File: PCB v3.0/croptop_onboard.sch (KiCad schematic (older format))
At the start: 100 parts, among them J15 TSM-112-01-L-DV, J16 DM3D-SF, Q4 BSS138, Q5 BSS138, Q6 BSS138, SW2 SW_Push, SW3 SW_Push, SW4 SW_Push, U30 TPD4E1U06DBV, U31 TPD4E1U06DBV, U32 AP22802AW5, U33 AP22802AW5, U34 TPD4E1U06DBV, U35 TPD4E1U06DBV, U36 AP22802AW5, U37 TPD4E1U06DBV, U38 TPD4E1U06DBV, U39 LIS3DSHTR, U40 CAM-M8C-0, U41 Si7006-A20

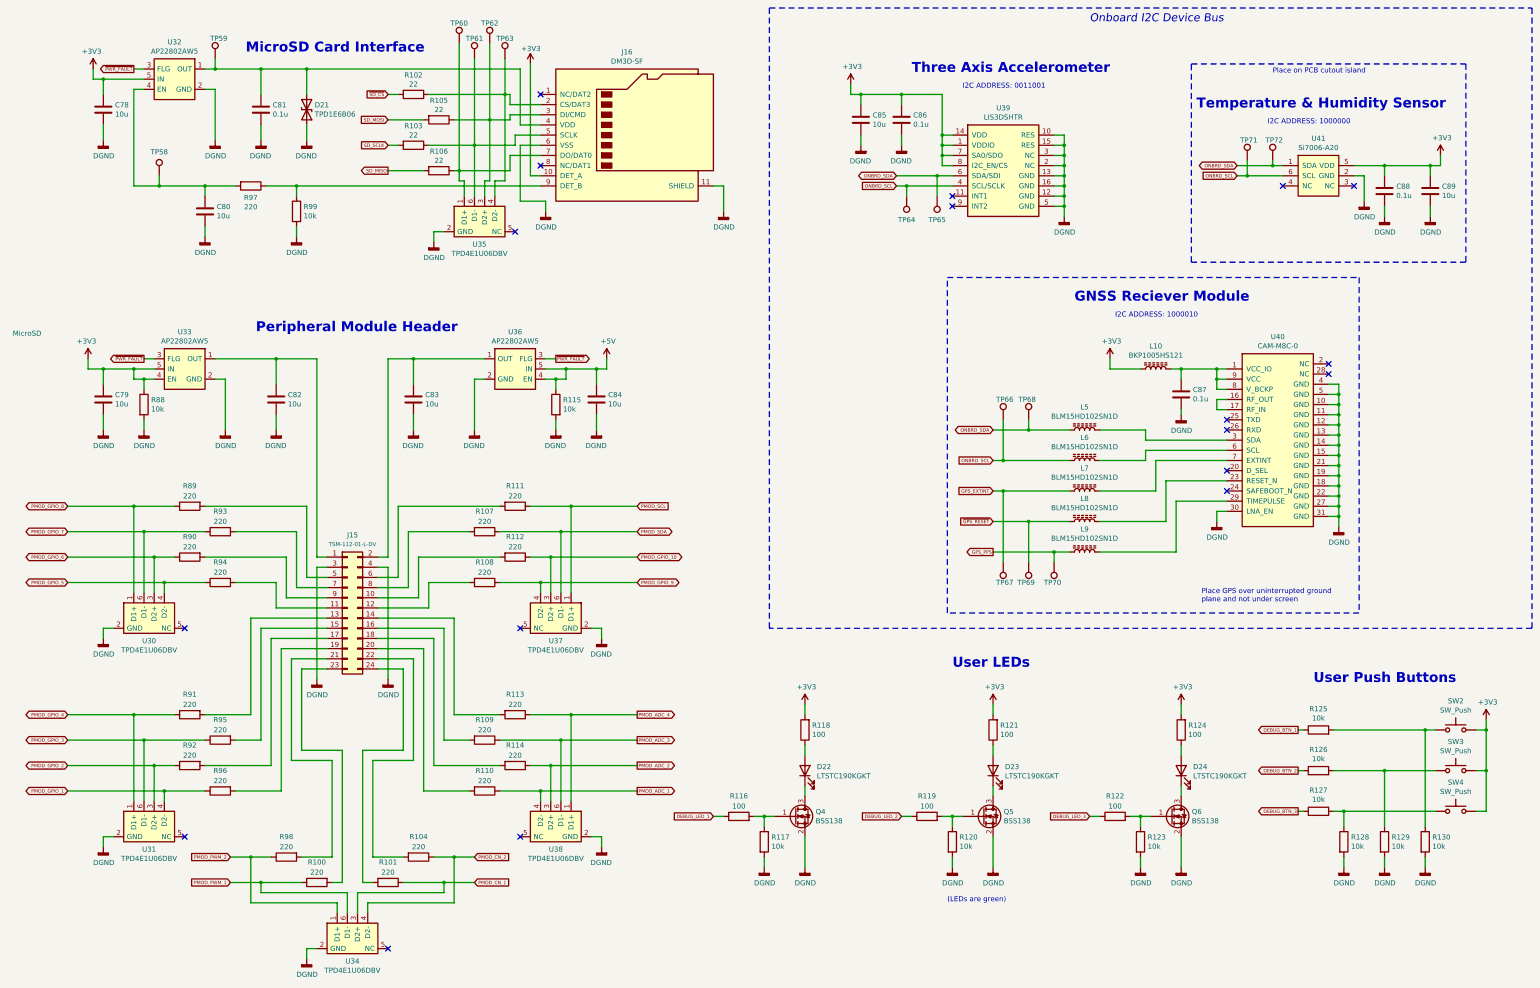
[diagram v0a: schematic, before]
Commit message: Updated PCB dimensions for Nextion screen, deleted old files
- Updated PCB v3.0 to use the Nextion screen mounting and connectors
- Deleted old I2CDriver files from /Software/
- Deleted unused /Software/Readme
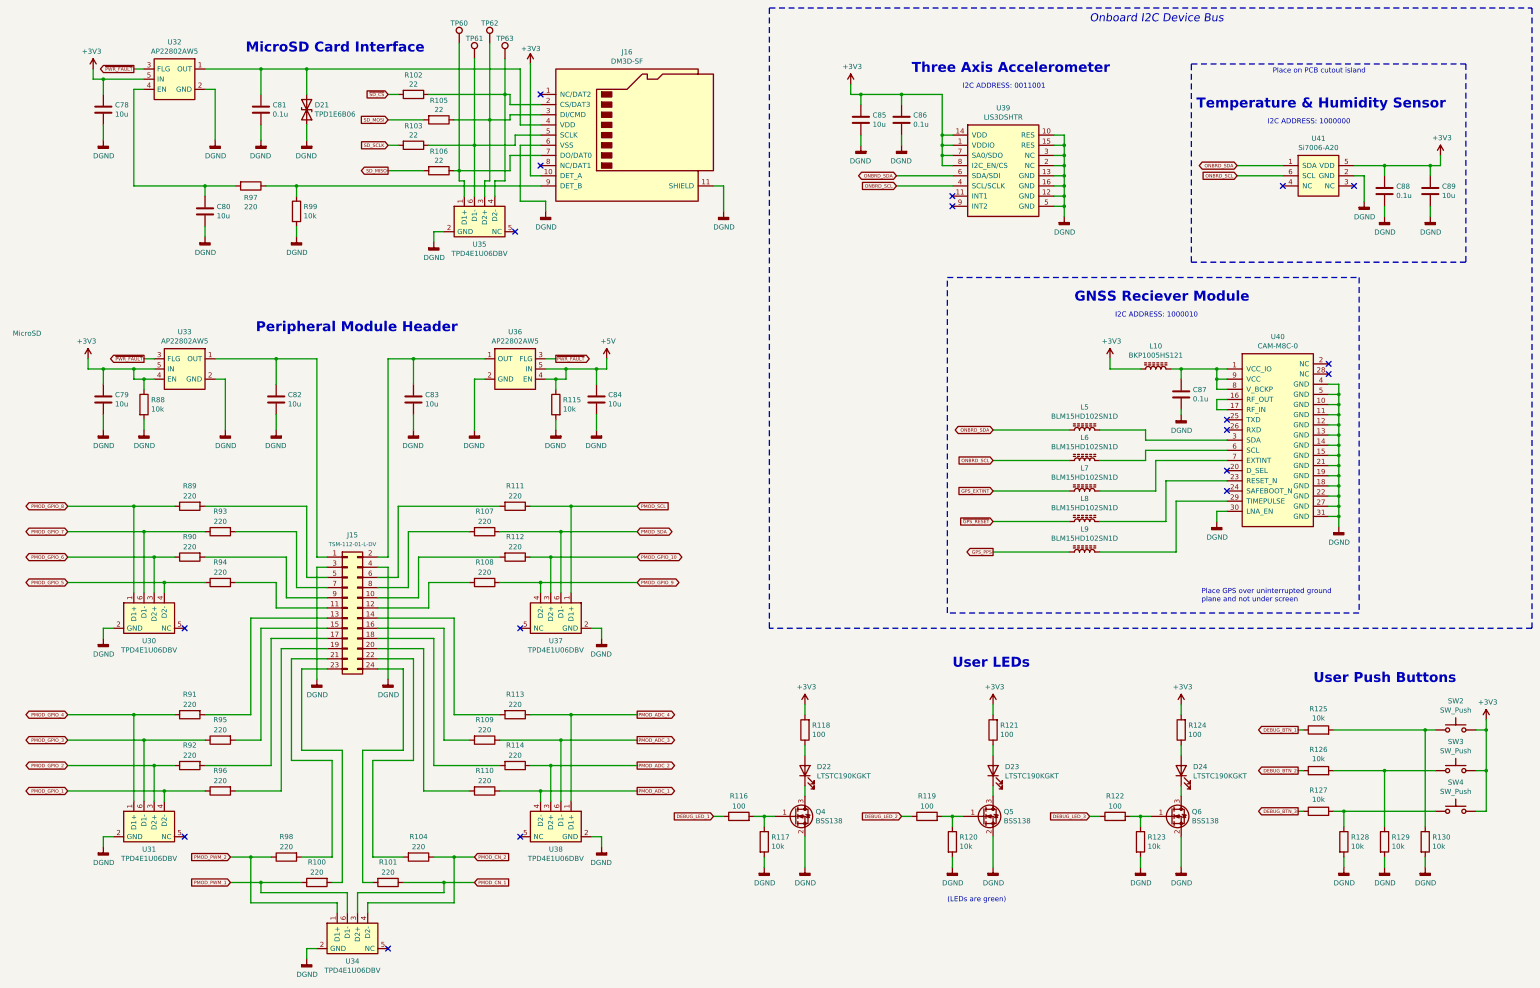
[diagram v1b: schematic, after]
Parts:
- removed TP58, TP59, TP64, TP65, TP66, TP67, TP68, TP69, TP70, TP71, TP72: TestPoint, TestPoint:TestPoint_Pad_D1.0mm, symbol Connector:TestPoint
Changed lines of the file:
@@
 $EndComp
 $Comp
-L CropTop:Si7006-A20 U41
-U 1 1 5CA090A6
-P 14050 2350
-F 0 "U41" H 14050 2717 50  0000 C CNN
-F 1 "Si7006-A20" H 14050 2626 50  0000 C CNN
-F 2 "croptop:SI7006" H 14050 2350 50  0001 C CNN
-F 3 "https://www.silabs.com/documents/public/data-sheets/Si7006-A20.pdf" H 14050 2350 50  0001 C CNN
-F 4 "SI7006-A20-IMR" H 14050 2350 50  0001 C CNN "MPN"
-	1    14050 2350
-	1    0    0    -1
-$EndComp
-$Comp
 L CropTop:DGND #PWR0227
 U 1 1 5CA022AE
@@
 	8100 2450 8200 2450
 $Comp
-L Connector:TestPoint TP?
-U 1 1 5CB78F40
-P 2650 2350
-AR Path="/64809F0C/5CB78F40" Ref="TP?"  Part="1"
-AR Path="/66A12230/5CB78F40" Ref="TP58"  Part="1"
-F 0 "TP58" H 2650 2584 50  0000 C CNN
-F 1 "TestPoint" H 2708 2379 50  0001 L CNN
-F 2 "TestPoint:TestPoint_Pad_D1.0mm" H 2850 2350 50  0001 C CNN
-F 3 "" H 2850 2350 50  0001 C CNN
-	1    2650 2350
-	1    0    0    -1
-$EndComp
-Wire Wire Line
-	2650 2350 2650 2450
-$Comp
 L CropTop:Micro_SD_Card_Det_0 J16
 U 1 1 5CBDF819
@@
 	2100 1850 2100 2000
 $Comp
-L Connector:TestPoint TP?
-U 1 1 5FDFF2C7
-P 3200 1200
-AR Path="/64809F0C/5FDFF2C7" Ref="TP?"  Part="1"
-AR Path="/66A12230/5FDFF2C7" Ref="TP59"  Part="1"
-AR Path="/64807BBC/5FDFF2C7" Ref="TP?"  Part="1"
-F 0 "TP59" H 3150 1400 50  0000 L CNN
-F 1 "TestPoint" H 3258 1229 50  0001 L CNN
-F 2 "TestPoint:TestPoint_Pad_D1.0mm" H 3400 1200 50  0001 C CNN
-F 3 "" H 3400 1200 50  0001 C CNN
-	1    3200 1200
-	1    0    0    -1
-$EndComp
-Wire Wire Line
-	3200 1200 3200 1300
-$Comp
 L CropTop:AP22802AW5 U?
 U 1 1 5FDFF2D1
@@
 Text GLabel 13250 2350 0    33   Input ~ 0
 ONBRD_SCL
-Wire Wire Line
-	13250 2250 13600 2250
-Wire Wire Line
-	13250 2350 13350 2350
 $Comp
 L CropTop:DGND #PWR?
@@
 Wire Wire Line
 	13050 5650 13050 5750
-Wire Wire Line
-	9900 2450 10000 2450
 $Comp
 L Device:L_Core_Ferrite L8
@@
 Wire Wire Line
 	12650 6050 11900 6050
-$Comp
-L Connector:TestPoint TP?
-U 1 1 5F92792B
-P 10950 6150
-AR Path="/64809F0C/5F92792B" Ref="TP?"  Part="1"
-AR Path="/66A12230/5F92792B" Ref="TP67"  Part="1"
-AR Path="/64807BBC/5F92792B" Ref="TP?"  Part="1"
-F 0 "TP67" H 10850 6350 50  0000 L CNN
-F 1 "TestPoint" H 11008 6179 50  0001 L CNN
-F 2 "TestPoint:TestPoint_Pad_D1.0mm" H 11150 6150 50  0001 C CNN
-F 3 "" H 11150 6150 50  0001 C CNN
-	1    10950 6150
-	-1   0    0    1
-$EndComp
-$Comp
-L Connector:TestPoint TP?
-U 1 1 5F927A3B
-P 10950 4750
-AR Path="/64809F0C/5F927A3B" Ref="TP?"  Part="1"
-AR Path="/66A12230/5F927A3B" Ref="TP66"  Part="1"
-AR Path="/64807BBC/5F927A3B" Ref="TP?"  Part="1"
-F 0 "TP66" H 10850 4950 50  0000 L CNN
-F 1 "TestPoint" H 11008 4779 50  0001 L CNN
-F 2 "TestPoint:TestPoint_Pad_D1.0mm" H 11150 4750 50  0001 C CNN
-F 3 "" H 11150 4750 50  0001 C CNN
-	1    10950 4750
-	-1   0    0    -1
-$EndComp
-$Comp
-L Connector:TestPoint TP?
-U 1 1 5F927CC0
-P 11200 6150
-AR Path="/64809F0C/5F927CC0" Ref="TP?"  Part="1"
-AR Path="/66A12230/5F927CC0" Ref="TP69"  Part="1"
-AR Path="/64807BBC/5F927CC0" Ref="TP?"  Part="1"
-F 0 "TP69" H 11310 6350 50  0000 R CNN
-F 1 "TestPoint" H 11258 6179 50  0001 L CNN
-F 2 "TestPoint:TestPoint_Pad_D1.0mm" H 11400 6150 50  0001 C CNN
-F 3 "" H 11400 6150 50  0001 C CNN
-	1    11200 6150
-	-1   0    0    1
-$EndComp
 Wire Wire Line
 	12450 5150 12450 5450
@@
 ~GPS_RESET
 $Comp
-L Connector:TestPoint TP?
-U 1 1 60F3FF7D
-P 10000 2550
-AR Path="/64809F0C/60F3FF7D" Ref="TP?"  Part="1"
-AR Path="/66A12230/60F3FF7D" Ref="TP64"  Part="1"
-AR Path="/64807BBC/60F3FF7D" Ref="TP?"  Part="1"
-F 0 "TP64" H 10000 2783 50  0000 C CNN
-F 1 "TestPoint" H 10058 2579 50  0001 L CNN
-F 2 "TestPoint:TestPoint_Pad_D1.0mm" H 10200 2550 50  0001 C CNN
-F 3 "" H 10200 2550 50  0001 C CNN
-	1    10000 2550
-	-1   0    0    1
-$EndComp
-Wire Wire Line
-	10000 2550 10000 2450
-Wire Wire Line
-	10300 2550 10300 2350
-$Comp
 L Device:Q_NMOS_GSD Q5
 U 1 1 6149971C
@@
 	2500 1500 2400 1500
 Wire Wire Line
-	2400 2450 2650 2450
-Wire Wire Line
 	2400 1500 2400 2450
 Wire Wire Line
@@
 	11550 2050 11550 2150
 Wire Wire Line
-	3200 1300 3650 1300
-Wire Wire Line
 	6300 2350 6400 2350
 Connection ~ 3650 1300
@@
 	4100 1550 4100 1300
 Connection ~ 4100 1300
-$Comp
-L Connector:TestPoint TP?
-U 1 1 5D227D71
-P 10300 2550
-AR Path="/64809F0C/5D227D71" Ref="TP?"  Part="1"
-AR Path="/66A12230/5D227D71" Ref="TP65"  Part="1"
-AR Path="/64807BBC/5D227D71" Ref="TP?"  Part="1"
-F 0 "TP65" H 10300 2783 50  0000 C CNN
-F 1 "TestPoint" H 10358 2579 50  0001 L CNN
-F 2 "TestPoint:TestPoint_Pad_D1.0mm" H 10500 2550 50  0001 C CNN
-F 3 "" H 10500 2550 50  0001 C CNN
-	1    10300 2550
-	-1   0    0    1
-$EndComp
-$Comp
-L Connector:TestPoint TP?
-U 1 1 5E1D1600
-P 13350 2200
-AR Path="/64809F0C/5E1D1600" Ref="TP?"  Part="1"
-AR Path="/66A12230/5E1D1600" Ref="TP71"  Part="1"
-AR Path="/64807BBC/5E1D1600" Ref="TP?"  Part="1"
-F 0 "TP71" H 13250 2400 50  0000 L CNN
-F 1 "TestPoint" H 13408 2229 50  0001 L CNN
-F 2 "TestPoint:TestPoint_Pad_D1.0mm" H 13550 2200 50  0001 C CNN
-F 3 "" H 13550 2200 50  0001 C CNN
-	1    13350 2200
-	-1   0    0    -1
-$EndComp
-$Comp
-L Connector:TestPoint TP?
-U 1 1 5E1D1607
-P 13600 2200
-AR Path="/64809F0C/5E1D1607" Ref="TP?"  Part="1"
-AR Path="/66A12230/5E1D1607" Ref="TP72"  Part="1"
-AR Path="/64807BBC/5E1D1607" Ref="TP?"  Part="1"
-F 0 "TP72" H 13500 2400 50  0000 L CNN
-F 1 "TestPoint" H 13658 2229 50  0001 L CNN
-F 2 "TestPoint:TestPoint_Pad_D1.0mm" H 13800 2200 50  0001 C CNN
-F 3 "" H 13800 2200 50  0001 C CNN
-	1    13600 2200
-	-1   0    0    -1
-$EndComp
-Wire Wire Line
-	13350 2200 13350 2350
-Connection ~ 13350 2350
-Wire Wire Line
-	13350 2350 13700 2350
-Wire Wire Line
-	13600 2200 13600 2250
-Connection ~ 13600 2250
-Wire Wire Line
-	13600 2250 13700 2250
-$Comp
-L Connector:TestPoint TP?
-U 1 1 5E571FC1
-P 11450 6150
-AR Path="/64809F0C/5E571FC1" Ref="TP?"  Part="1"
-AR Path="/66A12230/5E571FC1" Ref="TP70"  Part="1"
-AR Path="/64807BBC/5E571FC1" Ref="TP?"  Part="1"
-F 0 "TP70" H 11550 6350 50  0000 R CNN
-F 1 "TestPoint" H 11508 6179 50  0001 L CNN
-F 2 "TestPoint:TestPoint_Pad_D1.0mm" H 11650 6150 50  0001 C CNN
-F 3 "" H 11650 6150 50  0001 C CNN
-	1    11450 6150
-	-1   0    0    1
-$EndComp
 Wire Notes Line
 	10400 6650 10400 3350
@@
 NoConn ~ 10450 2550
 NoConn ~ 10450 2650
-Connection ~ 10000 2450
-Wire Wire Line
-	10000 2450 10450 2450
-Connection ~ 10300 2350
-Wire Wire Line
-	10300 2350 10450 2350
-Wire Wire Line
-	9900 2350 10300 2350
 Wire Wire Line
 	2100 1550 2100 1400
@@
 Wire Wire Line
 	6550 4150 6450 4150
-Wire Wire Line
-	3100 1300 3200 1300
-Connection ~ 3200 1300
-Wire Wire Line
-	3100 2450 2650 2450
 Connection ~ 3100 2450
-Connection ~ 2650 2450
 Wire Wire Line
 	4000 2450 6400 2450
@@
 Wire Wire Line
 	12000 4250 12300 4250
-$Comp
-L Connector:TestPoint TP?
-U 1 1 5E9FCD1E
-P 11200 4750
-AR Path="/64809F0C/5E9FCD1E" Ref="TP?"  Part="1"
-AR Path="/66A12230/5E9FCD1E" Ref="TP68"  Part="1"
-AR Path="/64807BBC/5E9FCD1E" Ref="TP?"  Part="1"
-F 0 "TP68" H 11100 4950 50  0000 L CNN
-F 1 "TestPoint" H 11258 4779 50  0001 L CNN
-F 2 "TestPoint:TestPoint_Pad_D1.0mm" H 11400 4750 50  0001 C CNN
-F 3 "" H 11400 4750 50  0001 C CNN
-	1    11200 4750
-	1    0    0    -1
-$EndComp
 NoConn ~ 13150 4750
 NoConn ~ 13150 4850
@@
 Wire Wire Line
 	12650 5550 13150 5550
-Wire Wire Line
-	10850 4850 11200 4850
-Wire Wire Line
-	10850 5150 10950 5150
-Wire Wire Line
-	10850 5450 10950 5450
-Wire Wire Line
-	10850 5750 11200 5750
-Wire Wire Line
-	10950 4750 10950 5150
-Connection ~ 10950 5150
-Wire Wire Line
-	10950 5150 11600 5150
-Wire Wire Line
-	11200 4750 11200 4850
-Connection ~ 11200 4850
-Wire Wire Line
-	11200 4850 11600 4850
-Wire Wire Line
-	11450 6050 11450 6150
-Wire Wire Line
-	11200 5750 11200 6150
-Connection ~ 11200 5750
-Wire Wire Line
-	11200 5750 11600 5750
-Wire Wire Line
-	10850 6050 11450 6050
-Wire Wire Line
-	10950 6150 10950 5450
-Connection ~ 10950 5450
-Wire Wire Line
-	10950 5450 11600 5450
-Connection ~ 11450 6050
-Wire Wire Line
-	11450 6050 11600 6050
 $Comp
 L Device:C C?
@@
 Text GLabel 7350 6350 2    33   BiDi ~ 0
 PMOD_GPIO_9
+Wire Wire Line
+	3100 1300 3650 1300
+Wire Wire Line
+	9900 2450 10450 2450
+Wire Wire Line
+	9900 2350 10450 2350
+Wire Wire Line
+	10850 5450 11600 5450
+Wire Wire Line
+	10850 5750 11600 5750
+Wire Wire Line
+	10850 6050 11600 6050
+Wire Wire Line
+	2400 2450 3100 2450
+$Comp
+L CropTop:Si7006-A20 U41
+U 1 1 5CA090A6
+P 14050 2350
+F 0 "U41" H 14050 2717 50  0000 C CNN
+F 1 "Si7006-A20" H 14050 2626 50  0000 C CNN
+F 2 "croptop:SI7006" H 14050 2350 50  0001 C CNN
+F 3 "https://www.silabs.com/documents/public/data-sheets/Si7006-A20.pdf" H 14050 2350 50  0001 C CNN
+F 4 "SI7006-A20-IMR" H 14050 2350 50  0001 C CNN "MPN"
+	1    14050 2350
+	1    0    0    -1
+$EndComp
+Wire Wire Line
+	13250 2350 13700 2350
+Wire Wire Line
+	13250 2250 13700 2250
+Wire Wire Line
+	10850 5150 11600 5150
+Wire Wire Line
+	10850 4850 11600 4850
 $EndSCHEMATC
